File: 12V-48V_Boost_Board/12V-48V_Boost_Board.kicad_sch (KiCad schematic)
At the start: 19 parts, among them J1 12V Input, J2 Input Current Sensing, J3 Output Current Sensing, J4 48V Output, J5 Output Measuring, U2 INA290

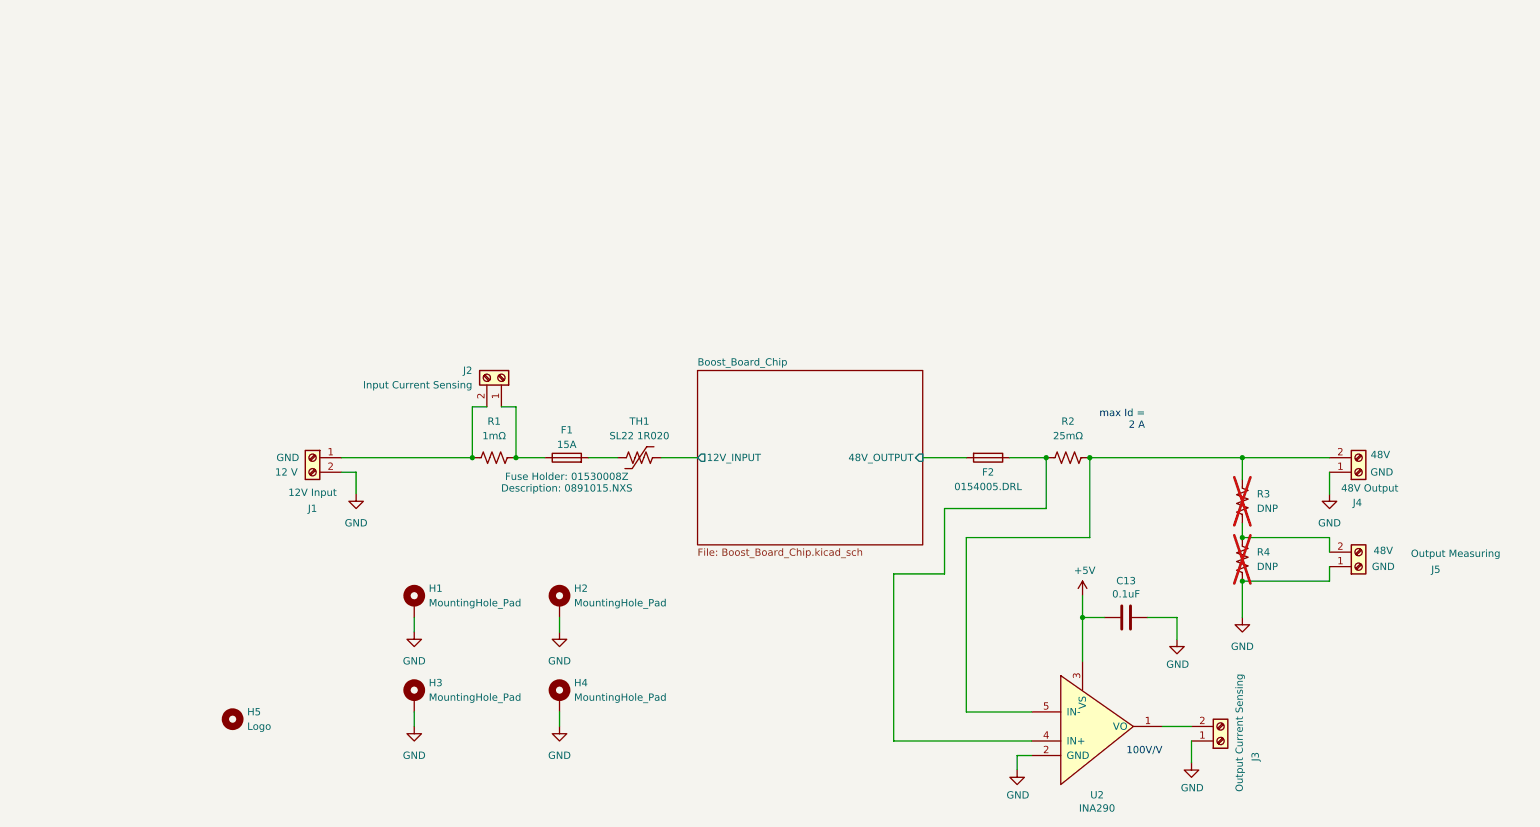
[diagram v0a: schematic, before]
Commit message: Added second op-amp, need to add 5 volt input
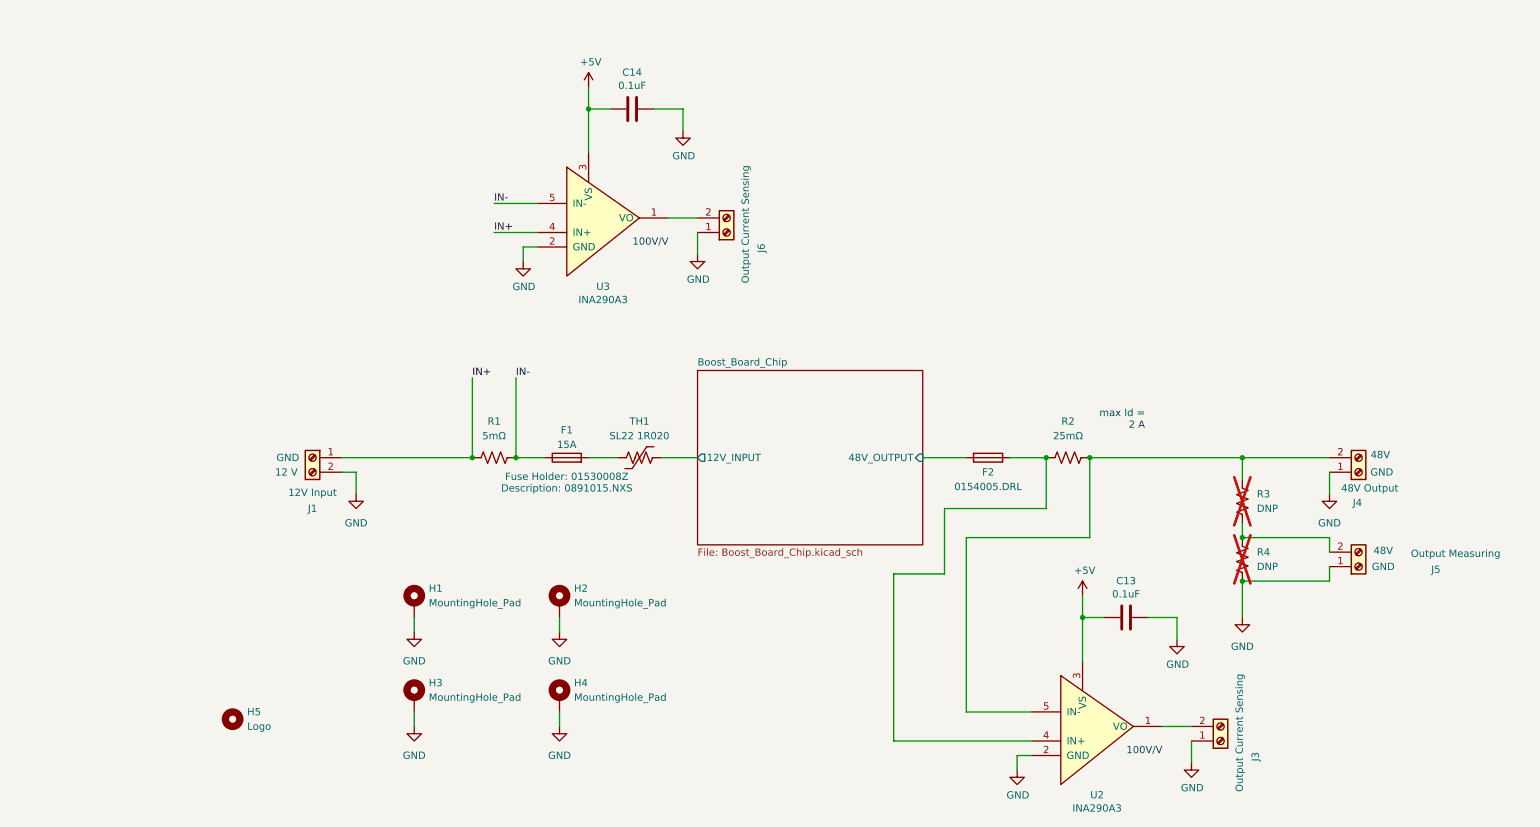
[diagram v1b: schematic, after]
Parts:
- removed J2: Input Current Sensing, TerminalBlock_Phoenix:TerminalBlock_Phoenix_PT-1,5-2-5.0-H_1x02_P5.00mm_Horizontal, symbol Connector:Screw_Terminal_01x02
- added C14: 0.1uF, Capacitor_SMD:C_0805_2012Metric_Pad1.18x1.45mm_HandSolder, symbol Device:C
- added J6: Output Current Sensing, TerminalBlock_Phoenix:TerminalBlock_Phoenix_PT-1,5-2-5.0-H_1x02_P5.00mm_Horizontal, symbol Connector:Screw_Terminal_01x02
- added U3: INA290A3, 12/48 boost:SC70-5_DCK_TEX, symbol canhw:INA180
- R1: value 1mΩ -> 5mΩ; footprint 12/48 boost:WSHM28181L000FEA -> Resistor_SMD:R_2816_7142Metric_Pad3.20x4.45mm_HandSolder
- U2: value INA290 -> INA290A3
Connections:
- net +5V: now also C14.2, U3.3 (VS)
- net GND: now also C14.1, J6.1 (Pin_1), U3.2 (GND)
- net IN-: now reaches F1.1, R1.2
- net IN-: now also U3.5 (IN-)
- net IN+: now reaches J1.1 (Pin_1), R1.1
- net IN+: now also U3.4 (IN+)
- new net: J6.2 (Pin_2), U3.1 (VO)

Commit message: Schematic and PCB changes. See descp.
- Added 12V to 5V LDO to schematic and PCB.
- Via stitched large planes both due to thermal and GND return path concerns.
- Other minor tweaks.
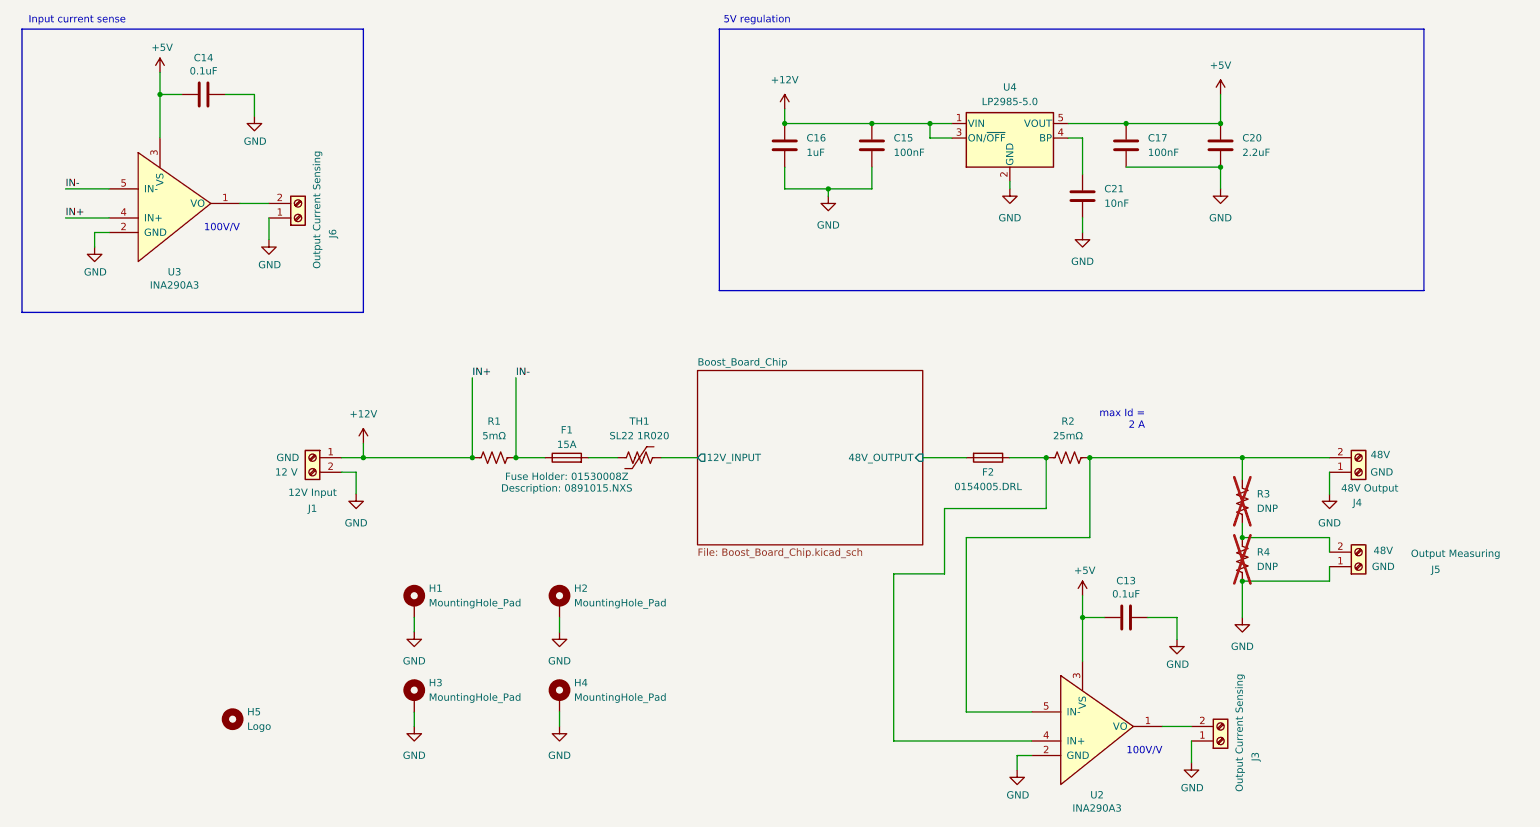
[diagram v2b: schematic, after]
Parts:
- added C15, C17: 100nF, Capacitor_SMD:C_0805_2012Metric_Pad1.18x1.45mm_HandSolder, symbol Device:C
- added C16: 1uF, Capacitor_SMD:C_0805_2012Metric_Pad1.18x1.45mm_HandSolder, symbol Device:C
- added C20: 2.2uF, Capacitor_SMD:C_0805_2012Metric_Pad1.18x1.45mm_HandSolder, symbol Device:C
- added C21: 10nF, Capacitor_SMD:C_0805_2012Metric_Pad1.18x1.45mm_HandSolder, symbol Device:C
- added U4: LP2985-5.0, Package_TO_SOT_SMD:SOT-23-5, symbol Regulator_Linear:LP2985-5.0
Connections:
- net +5V: now also C17.1, C20.1, U4.5 (VOUT)
- net GND: now also C15.2, C16.2, C17.2, C20.2, C21.2, U4.2 (GND)
- net IN+ renamed +12V
- net +12V: now also C15.1, C16.1, U4.1 (VIN), U4.3 (ON/~{OFF})
- new net: C21.1, U4.4 (BP)
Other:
- note added: "5V regulation"
- note added: "Input current sense"
- moved on the sheet: C14, J6, U3

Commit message: Moved current sense amps. Other minor changes.
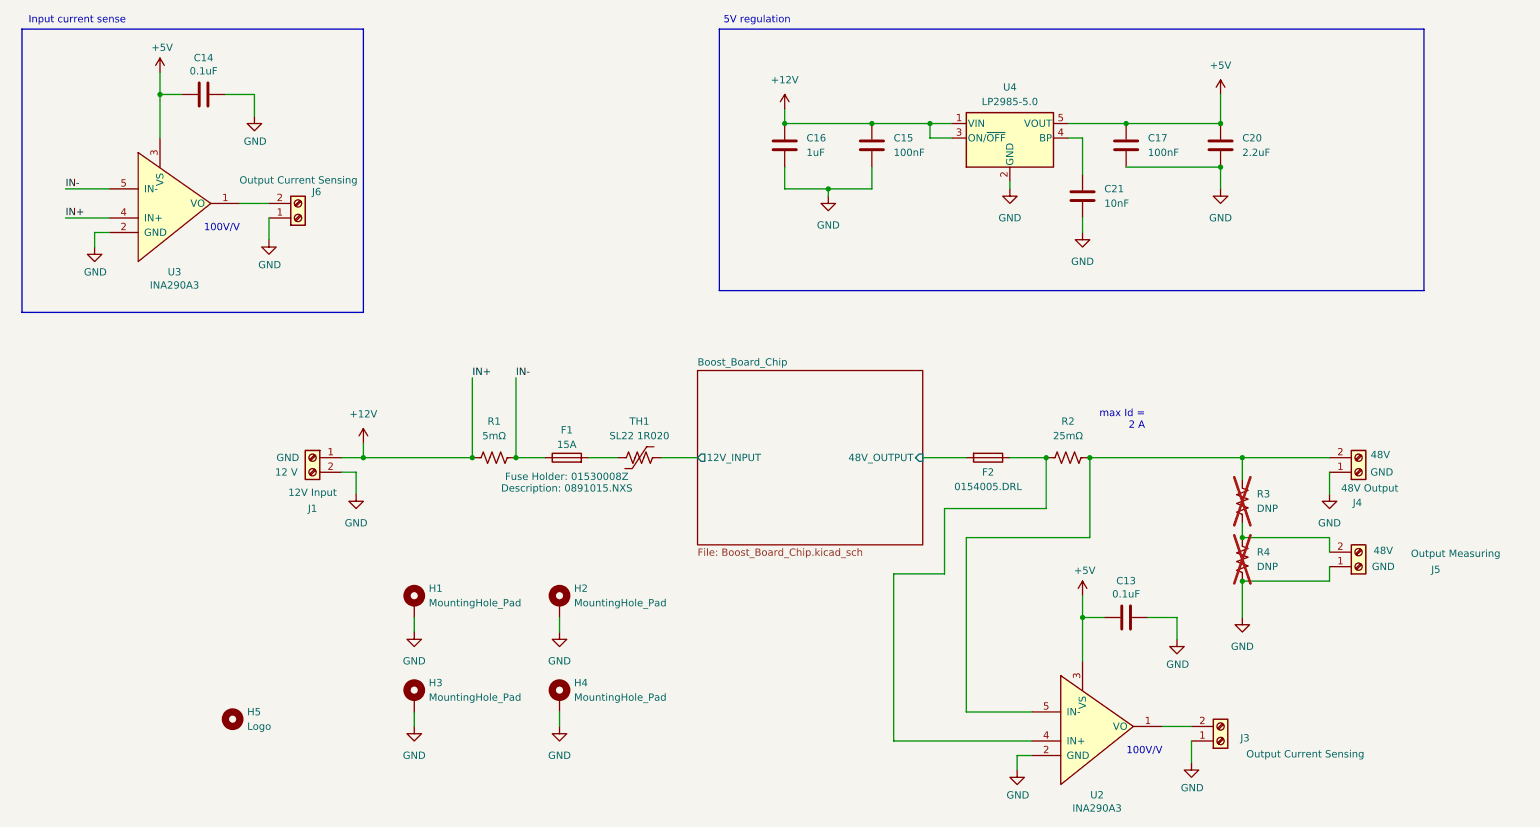
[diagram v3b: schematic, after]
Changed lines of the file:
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@@
 		(dnp no)
 		(property "Reference" "J3"
-			(at 235.966 152.146 90)
+			(at 234.95 148.082 0)
 			(effects
 				(font
@@
 		)
 		(property "Value" "Output Current Sensing"
-			(at 233.172 157.48 90)
+			(at 255.016 150.876 0)
 			(effects
 				(font
@@
 		(dnp no)
 		(property "Reference" "J6"
-			(at 74.676 60.706 90)
+			(at 72.644 52.578 0)
 			(effects
 				(font
@@
 		)
 		(property "Value" "Output Current Sensing"
-			(at 71.882 66.04 90)
+			(at 78.994 50.546 0)
 			(effects
 				(font
